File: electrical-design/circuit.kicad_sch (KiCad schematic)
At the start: 48 parts, among them J1 AVR-ISP-10, J2 Analoge Header, Q1 2N3906, Q2 2N3906, Q3 2N3906, Q4 2N3906, SW1 Reset Button, SW2 SW_DIP_x04, SW3 Reset Button, U1 ATmega8A-P, U2 LTC-4627JD, U3 NE555P, Y1 16MHz

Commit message: Completed Design For Rev 1.0
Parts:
- added C7: 33uF, Capacitor_THT:CP_Radial_D4.0mm_P1.50mm, symbol Device:C_Polarized_US
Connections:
- net GND: now also C7.2
- net VCC: now also C7.1
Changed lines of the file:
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@@
   (junction (at 233.68 39.37) (diameter 0) (color 0 0 0 0)
   )
+  (junction (at 35.56 157.48) (diameter 0) (color 0 0 0 0)
+  )
   (junction (at 233.68 67.31) (diameter 0) (color 0 0 0 0)
   )
   (junction (at 158.75 62.23) (diameter 0) (color 0 0 0 0)
+  )
+  (junction (at 35.56 128.27) (diameter 0) (color 0 0 0 0)
   )
   (junction (at 48.26 40.64) (diameter 0) (color 0 0 0 0)
@@
     (stroke (width 0) (type default))
   )
+  (wire (pts (xy 17.78 132.08) (xy 17.78 128.27))
+    (stroke (width 0) (type default))
+  )
   (wire (pts (xy 161.29 19.05) (xy 161.29 31.75))
     (stroke (width 0) (type default))
@@
     (stroke (width 0) (type default))
   )
+  (wire (pts (xy 17.78 128.27) (xy 35.56 128.27))
+    (stroke (width 0) (type default))
+  )
   (wire (pts (xy 158.75 55.88) (xy 158.75 62.23))
     (stroke (width 0) (type default))
@@
     (stroke (width 0) (type default))
   )
+  (wire (pts (xy 35.56 128.27) (xy 35.56 133.35))
+    (stroke (width 0) (type default))
+  )
   (wire (pts (xy 81.28 53.34) (xy 86.36 53.34))
     (stroke (width 0) (type default))
@@
     (stroke (width 0) (type default))
   )
-  (wire (pts (xy 35.56 129.54) (xy 35.56 133.35))
+  (wire (pts (xy 35.56 123.19) (xy 35.56 128.27))
     (stroke (width 0) (type default))
   )
@@
     (stroke (width 0) (type default))
   )
+  (wire (pts (xy 17.78 157.48) (xy 35.56 157.48))
+    (stroke (width 0) (type default))
+  )
+  (wire (pts (xy 35.56 157.48) (xy 35.56 158.75))
+    (stroke (width 0) (type default))
+  )
   (wire (pts (xy 151.13 140.97) (xy 166.37 140.97))
     (stroke (width 0) (type default))
@@
     (stroke (width 0) (type default))
   )
+  (wire (pts (xy 17.78 139.7) (xy 17.78 157.48))
+    (stroke (width 0) (type default))
+  )
   (wire (pts (xy 105.41 151.13) (xy 110.49 151.13))
     (stroke (width 0) (type default))
@@
     (stroke (width 0) (type default))
   )
-  (wire (pts (xy 35.56 156.21) (xy 35.56 158.75))
+  (wire (pts (xy 35.56 156.21) (xy 35.56 157.48))
     (stroke (width 0) (type default))
   )
@@
     )
   )
+  (symbol (lib_id "Device:C_Polarized_US") (at 17.78 135.89 0) (unit 1)
+    (in_bom yes) (on_board yes) (dnp no) (fields_autoplaced)
+    (property "Reference" "C7" (at 21.59 134.62 0)
+      (effects (font (size 1.27 1.27)) (justify left))
+    )
+    (property "Value" "33uF" (at 21.59 137.16 0)
+      (effects (font (size 1.27 1.27)) (justify left))
+    )
+    (property "Footprint" "Capacitor_THT:CP_Radial_D4.0mm_P1.50mm" (at 17.78 135.89 0)
+      (effects (font (size 1.27 1.27)) hide)
+    )
+    (property "Datasheet" "~" (at 17.78 135.89 0)
+      (effects (font (size 1.27 1.27)) hide)
+    )
+    (pin "1")
+    (pin "2")
+    (instances
+      (project "circuit"
+        (path "/e92f8e40-1e47-4cd0-a865-c589067a003b"
+          (reference "C7") (unit 1)
+        )
+      )
+    )
+  )
   (symbol (lib_id "power:GND") (at 20.32 67.31 0) (unit 1)
     (in_bom yes) (on_board yes) (dnp no) (fields_autoplaced)
@@
     )
   )
-  (symbol (lib_id "power:VCC") (at 35.56 129.54 0) (unit 1)
-    (in_bom yes) (on_board yes) (dnp no) (fields_autoplaced)
-    (property "Reference" "#PWR03" (at 35.56 133.35 0)
-      (effects (font (size 1.27 1.27)) hide)
-    )
-    (property "Value" "VCC" (at 35.56 124.46 0)
-      (effects (font (size 1.27 1.27)))
-    )
-    (property "Footprint" "" (at 35.56 129.54 0)
-      (effects (font (size 1.27 1.27)) hide)
-    )
-    (property "Datasheet" "" (at 35.56 129.54 0)
-      (effects (font (size 1.27 1.27)) hide)
-    )
+  (symbol (lib_id "power:VCC") (at 35.56 123.19 0) (unit 1)
+    (in_bom yes) (on_board yes) (dnp no) (fields_autoplaced)
+    (property "Reference" "#PWR03" (at 35.56 127 0)
+      (effects (font (size 1.27 1.27)) hide)
+    )
+    (property "Value" "VCC" (at 35.56 118.11 0)
+      (effects (font (size 1.27 1.27)))
+    )
+    (property "Footprint" "" (at 35.56 123.19 0)
+      (effects (font (size 1.27 1.27)) hide)
+    )
+    (property "Datasheet" "" (at 35.56 123.19 0)
+      (effects (font (size 1.27 1.27)) hide)
+    )

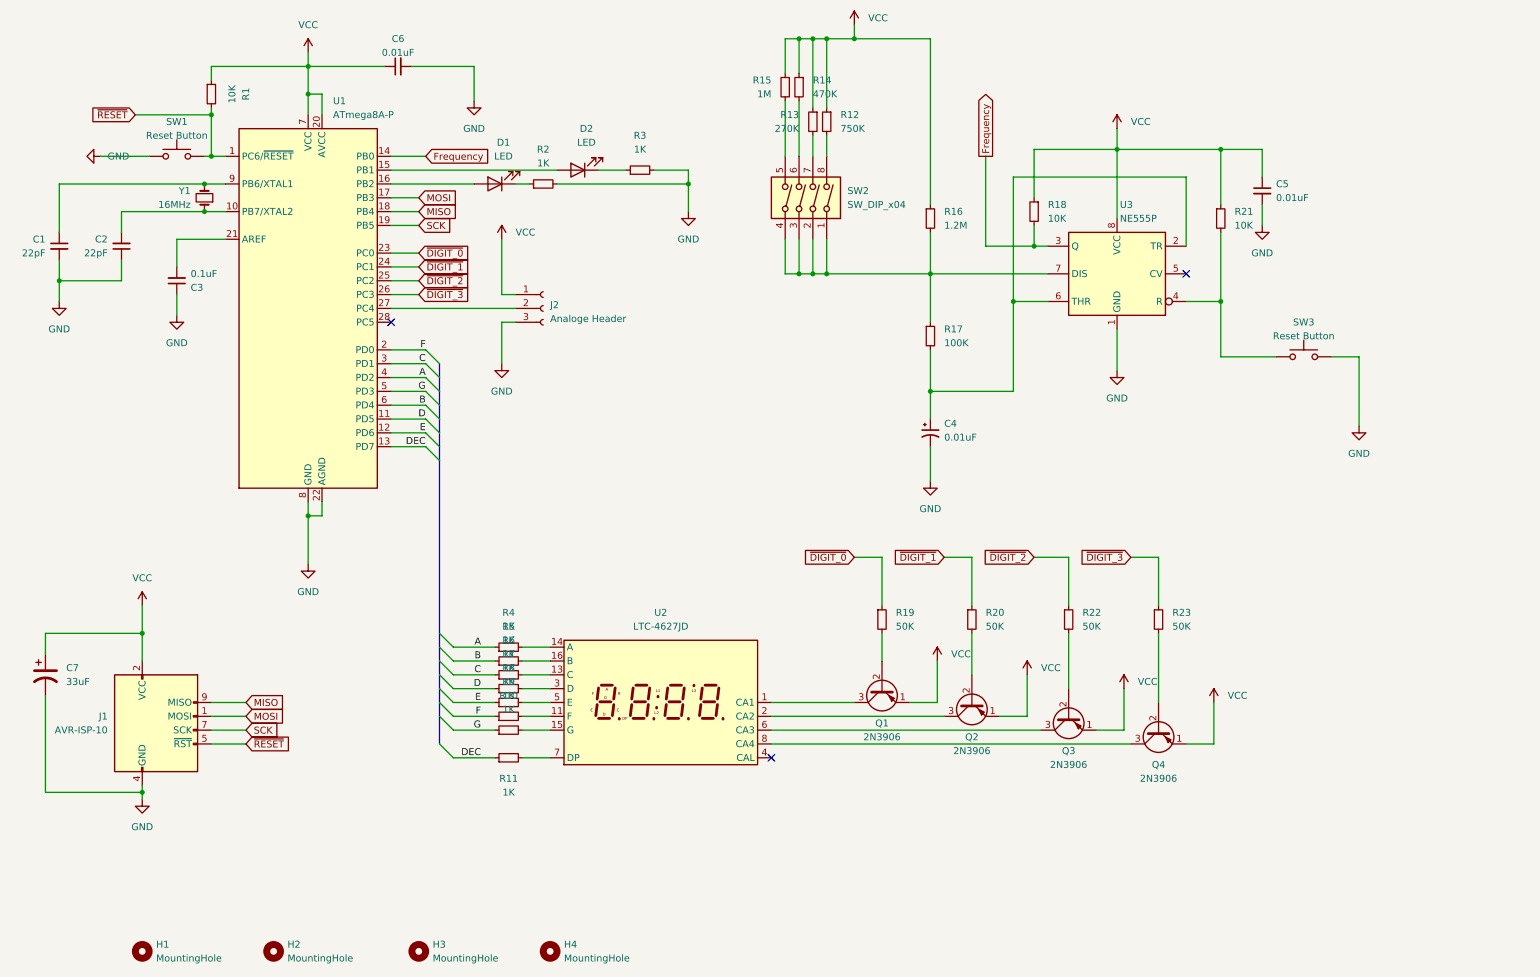
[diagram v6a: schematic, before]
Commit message: Created Parts Order List And Modified PCB Rev 1.0 Accordingly
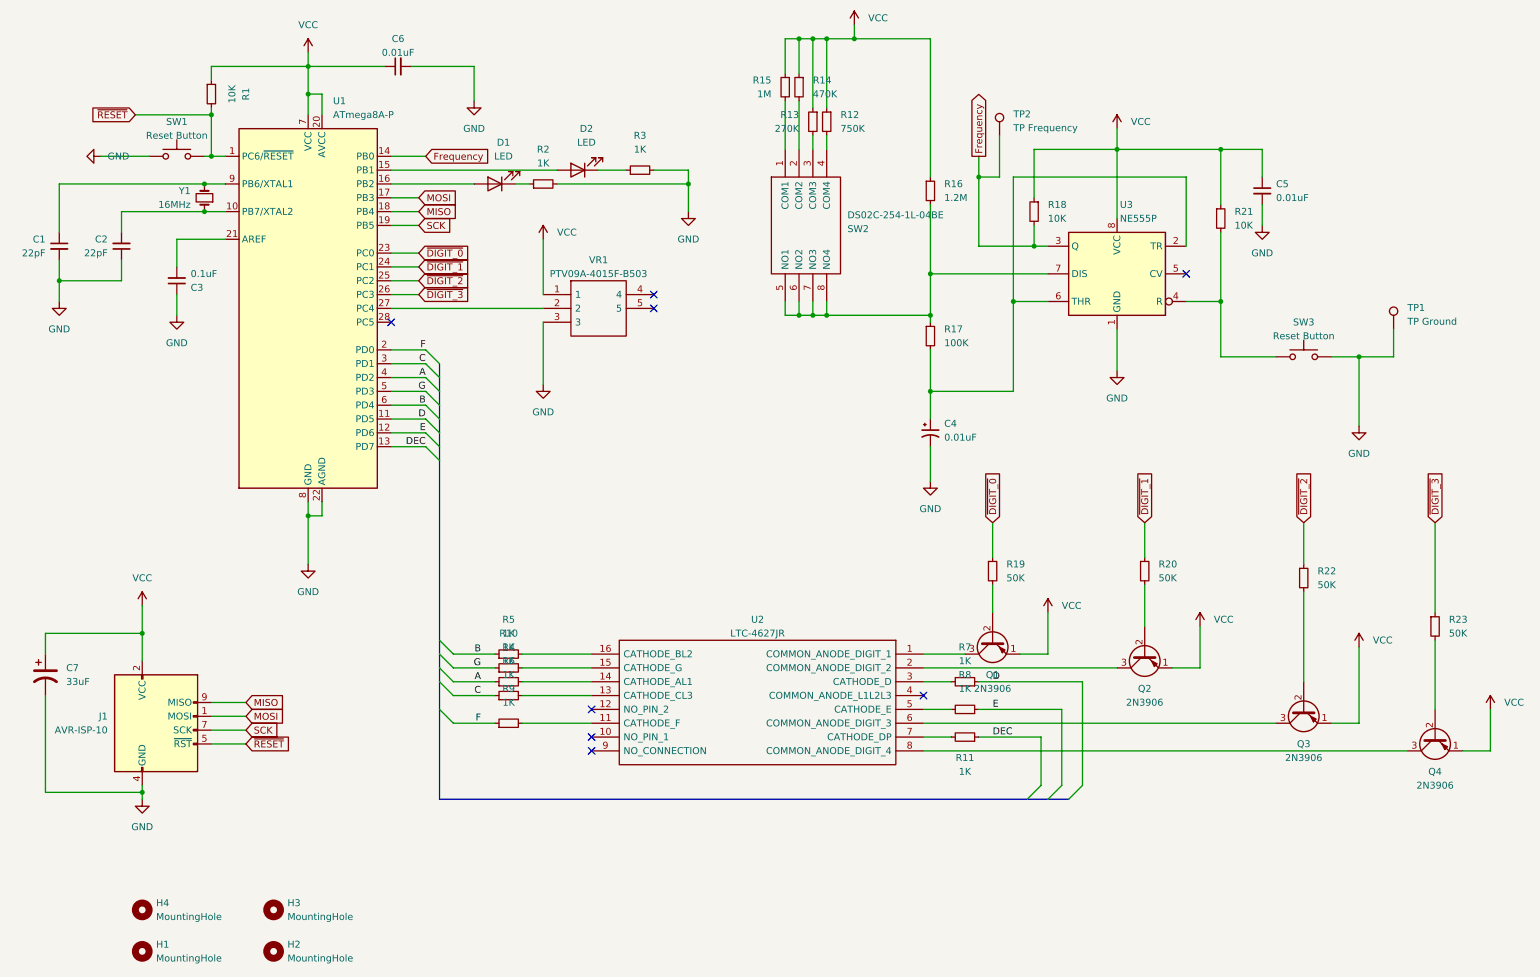
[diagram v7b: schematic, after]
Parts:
- removed J2: Analoge Header, Connector_JST:JST_XH_B3B-XH-A_1x03_P2.50mm_Vertical, symbol Connector:Conn_01x03_Female
- removed SW2: SW_DIP_x04, Button_Switch_THT:SW_DIP_SPSTx04_Slide_9.78x12.34mm_W7.62mm_P2.54mm, symbol Switch:SW_DIP_x04
- removed U2: LTC-4627JD, Display_7Segment:LTC-4627Jx, symbol Display_Character:LTC-4627JD
- added SW2: DS02C-254-1L-04BE, DS02C2541L04BE, symbol DIP Switch:DS02C-254-1L-04BE
- added TP1: TP Ground, TestPoint:TestPoint_THTPad_2.0x2.0mm_Drill1.0mm, symbol Connector:TestPoint
- added TP2: TP Frequency, TestPoint:TestPoint_THTPad_2.0x2.0mm_Drill1.0mm, symbol Connector:TestPoint
- added U2: LTC-4627JR, 7 Segment Display:DIPS1016W50P254L4018H725Q16N, symbol 7 Segment Display:LTC-4627JR
- added VR1: PTV09A-4015F-B503, PTV09A4020FB103, symbol Potentiometer:PTV09A-4015F-B503
- C7: footprint Capacitor_THT:CP_Radial_D4.0mm_P1.50mm -> Capacitor_THT:CP_Radial_D4.0mm_P2.00mm
- H1, H2, H3, H4: now left out of the parts list
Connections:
- net Frequency: now also TP2.1
- net GND: now also TP1.1, VR1.3
- net VCC: now also VR1.1
- net at R9.2: now also U2.11 (CATHODE_F)
- net at U1.27 (PC4): now also VR1.2
- net at R16.2, R17.1, U3.7 (DIS): now also SW2.5 (NO1), SW2.6 (NO2), SW2.7 (NO3), SW2.8 (NO4)
- net at R15.2: now also SW2.1 (COM1)
- net at R14.2: now also SW2.2 (COM2)
- net at R13.2: now also SW2.3 (COM3)
- net at R12.2: now also SW2.4 (COM4)
- net at R4.2: now also U2.14 (CATHODE_AL1)
- net at R6.2: now also U2.13 (CATHODE_CL3)
- net at Q2.3 (C): now also U2.2 (COMMON_ANODE_DIGIT_2)
- net at R5.2: now also U2.16 (CATHODE_BL2)
- net at Q4.3 (C): now also U2.8 (COMMON_ANODE_DIGIT_4)
- net at Q1.3 (C): now also U2.1 (COMMON_ANODE_DIGIT_1)
- net at R10.2: now also U2.15 (CATHODE_G)
- net at R7.2: now also U2.3 (CATHODE_D)
- net at R8.2: now also U2.5 (CATHODE_E)
- net at Q3.3 (C): now also U2.6 (COMMON_ANODE_DIGIT_3)
- net at R11.2: now also U2.7 (CATHODE_DP)
- no-connect marks 3 -> 8
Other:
- moved on the sheet: H3, H4, Q1, Q2, Q3, Q4, R10, R11, R16, R19, R20, R22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

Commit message: Send R1.0 to Production
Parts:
- added R24, R25: 1K, Resistor_THT:R_Axial_DIN0204_L3.6mm_D1.6mm_P5.08mm_Horizontal, symbol Device:R_Small
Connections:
- net GND: now also R25.1; no longer VR1.3
- net VCC: now also R24.1; no longer VR1.1
- new net: R25.2, VR1.3
- new net: R24.2, VR1.1
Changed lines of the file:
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@@
+    (stroke (width 0) (type default))
+  )
+  (wire (pts (xy 109.22 71.12) (xy 109.22 74.93))
     (stroke (width 0) (type default))
   )
@@
     (stroke (width 0) (type default))
   )
-  (wire (pts (xy 109.22 66.04) (xy 109.22 55.88))
-    (stroke (width 0) (type default))
-  )
   (wire (pts (xy 196.85 132.08) (xy 201.93 132.08))
     (stroke (width 0) (type default))
@@
     (stroke (width 0) (type default))
   )
+  (wire (pts (xy 109.22 80.01) (xy 109.22 83.82))
+    (stroke (width 0) (type default))
+  )
+  (wire (pts (xy 109.22 60.96) (xy 109.22 66.04))
+    (stroke (width 0) (type default))
+  )
   (wire (pts (xy 48.26 146.05) (xy 54.61 146.05))
     (stroke (width 0) (type default))
@@
     (stroke (width 0) (type default))
   )
-  (wire (pts (xy 109.22 71.12) (xy 109.22 82.55))
-    (stroke (width 0) (type default))
-  )
   (wire (pts (xy 156.21 19.05) (xy 158.75 19.05))
     (stroke (width 0) (type default))
@@
     (stroke (width 0) (type default))
   )
+  (wire (pts (xy 109.22 52.07) (xy 109.22 55.88))
+    (stroke (width 0) (type default))
+  )
   (wire (pts (xy 46.99 45.72) (xy 50.8 45.72))
     (stroke (width 0) (type default))
   )
+  (wire (pts (xy 109.22 83.82) (xy 120.65 83.82))
+    (stroke (width 0) (type default))
+  )
   (wire (pts (xy 119.38 43.18) (xy 124.46 43.18))
     (stroke (width 0) (type default))
@@
   )
   (wire (pts (xy 105.41 134.62) (xy 118.11 134.62))
+    (stroke (width 0) (type default))
+  )
+  (wire (pts (xy 109.22 52.07) (xy 119.38 52.07))
     (stroke (width 0) (type default))
   )
@@
     )
   )
-  (symbol (lib_id "power:VCC") (at 109.22 55.88 0) (unit 1)
-    (in_bom yes) (on_board yes) (dnp no) (fields_autoplaced)
-    (property "Reference" "#PWR08" (at 109.22 59.69 0)
-      (effects (font (size 1.27 1.27)) hide)
-    )
-    (property "Value" "VCC" (at 111.76 54.6099 0)
-      (effects (font (size 1.27 1.27)) (justify left))
-    )
-    (property "Footprint" "" (at 109.22 55.88 0)
-      (effects (font (size 1.27 1.27)) hide)
-    )
-    (property "Datasheet" "" (at 109.22 55.88 0)
-      (effects (font (size 1.27 1.27)) hide)
-    )
-    (pin "1")
-    (instances
-      (project "circuit"
-        (path "/e92f8e40-1e47-4cd0-a865-c589067a003b"
-          (reference "#PWR08") (unit 1)
-        )
-      )
-    )
-  )
   (symbol (lib_id "Device:R_Small") (at 161.29 34.29 0) (mirror y) (unit 1)
     (in_bom yes) (on_board yes) (dnp no) (fields_autoplaced)
@@
     )
   )
-  (symbol (lib_id "power:GND") (at 109.22 82.55 0) (unit 1)
-    (in_bom yes) (on_board yes) (dnp no)
-    (property "Reference" "#PWR09" (at 109.22 88.9 0)
-      (effects (font (size 1.27 1.27)) hide)
-    )
-    (property "Value" "GND" (at 109.22 87.63 0)
-      (effects (font (size 1.27 1.27)))
-    )
-    (property "Footprint" "" (at 109.22 82.55 0)
-      (effects (font (size 1.27 1.27)) hide)
-    )
-    (property "Datasheet" "" (at 109.22 82.55 0)
-      (effects (font (size 1.27 1.27)) hide)
-    )
-    (pin "1")
-    (instances
-      (project "circuit"
-        (path "/e92f8e40-1e47-4cd0-a865-c589067a003b"
-          (reference "#PWR09") (unit 1)
-        )
-      )
-    )
-  )
   (symbol (lib_id "power:GND") (at 27.94 40.64 270) (unit 1)
     (in_bom yes) (on_board yes) (dnp no) (fields_autoplaced)
@@
     )
   )
+  (symbol (lib_id "Device:R_Small") (at 109.22 77.47 180) (unit 1)
+    (in_bom yes) (on_board yes) (dnp no) (fields_autoplaced)
+    (property "Reference" "R25" (at 111.76 76.835 0)
+      (effects (font (size 1.27 1.27)) (justify right))
+    )
+    (property "Value" "1K" (at 111.76 79.375 0)
+      (effects (font (size 1.27 1.27)) (justify right))
+    )
+    (property "Footprint" "Resistor_THT:R_Axial_DIN0204_L3.6mm_D1.6mm_P5.08mm_Horizontal" (at 109.22 77.47 0)
+      (effects (font (size 1.27 1.27)) hide)
+    )
+    (property "Datasheet" "~" (at 109.22 77.47 0)
+      (effects (font (size 1.27 1.27)) hide)
+    )
+    (pin "1")
+    (pin "2")
+    (instances
+      (project "circuit"
+        (path "/e92f8e40-1e47-4cd0-a865-c589067a003b"
+          (reference "R25") (unit 1)
+        )
+      )
+    )
+  )
   (symbol (lib_id "Potentiometer:PTV09A-4015F-B503") (at 109.22 66.04 0) (unit 1)
     (in_bom yes) (on_board yes) (dnp no) (fields_autoplaced)
@@
     )
   )
+  (symbol (lib_id "power:VCC") (at 119.38 52.07 270) (unit 1)
+    (in_bom yes) (on_board yes) (dnp no) (fields_autoplaced)
+    (property "Reference" "#PWR08" (at 115.57 52.07 0)
+      (effects (font (size 1.27 1.27)) hide)
+    )
+    (property "Value" "VCC" (at 120.6501 54.61 0)
+      (effects (font (size 1.27 1.27)) (justify left))
+    )
+    (property "Footprint" "" (at 119.38 52.07 0)
+      (effects (font (size 1.27 1.27)) hide)
+    )
+    (property "Datasheet" "" (at 119.38 52.07 0)
+      (effects (font (size 1.27 1.27)) hide)
+    )
+    (pin "1")
+    (instances
+      (project "circuit"
+        (path "/e92f8e40-1e47-4cd0-a865-c589067a003b"
+          (reference "#PWR08") (unit 1)
+        )
+      )
+    )
+  )
   (symbol (lib_id "Device:R_Small") (at 109.22 45.72 90) (unit 1)
     (in_bom yes) (on_board yes) (dnp no) (fields_autoplaced)
@@
         (path "/e92f8e40-1e47-4cd0-a865-c589067a003b"
           (reference "R2") (unit 1)
+        )
+      )
+    )
+  )
+  (symbol (lib_id "power:GND") (at 120.65 83.82 90) (unit 1)
+    (in_bom yes) (on_board yes) (dnp no)
+    (property "Reference" "#PWR09" (at 127 83.82 0)
+      (effects (font (size 1.27 1.27)) hide)
+    )
+    (property "Value" "GND" (at 125.73 83.82 0)
+      (effects (font (size 1.27 1.27)))
+    )
+    (property "Footprint" "" (at 120.65 83.82 0)
+      (effects (font (size 1.27 1.27)) hide)
+    )
+    (property "Datasheet" "" (at 120.65 83.82 0)
+      (effects (font (size 1.27 1.27)) hide)
+    )
+    (pin "1")
+    (instances
+      (project "circuit"
+        (path "/e92f8e40-1e47-4cd0-a865-c589067a003b"
+          (reference "#PWR09") (unit 1)
         )
       )
@@
         )
       )
+    )
+  )
+  (symbol (lib_id "Device:R_Small") (at 109.22 58.42 0) (mirror y) (unit 1)
+    (in_bom yes) (on_board yes) (dnp no)
+    (property "Reference" "R24" (at 111.76 59.055 0)
+      (effects (font (size 1.27 1.27)) (justify right))
+    )
+    (property "Value" "1K" (at 111.76 56.515 0)
+      (effects (font (size 1.27 1.27)) (justify right))
+    )
+    (property "Footprint" "Resistor_THT:R_Axial_DIN0204_L3.6mm_D1.6mm_P5.08mm_Horizontal" (at 109.22 58.42 0)
+      (effects (font (size 1.27 1.27)) hide)
+    )
+    (property "Datasheet" "~" (at 109.22 58.42 0)
+      (effects (font (size 1.27 1.27)) hide)
+    )
+    (pin "1")
+    (pin "2")
+    (instances
+      (project "circuit"
+        (path "/e92f8e40-1e47-4cd0-a865-c589067a003b"
+          (reference "R24") (unit 1)
+        )
+      )
